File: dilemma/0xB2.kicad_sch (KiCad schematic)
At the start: 106 parts, among them J1 USB_C_Receptacle_USB2.0, J101 trackball, J102 Serial, J103 Serial, J104 BATTERY_CONN_DEANS, J105 S3B-PH-SM4-TB(LF)(SN), J106 S3B-PH-SM4-TB(LF)(SN), J107 Conn_01x08_Female, J113 Cirque, J5 Conn_01x02, SW1 SW_Push, SW101 SW_Push, SW102 SW_Push, SW103 SW_Push, SW104 SW_Push, SW105 SW_Push, SW106 SW_Push, SW107 SW_Push, SW108 SW_Push, SW109 SW_Push, SW110 SW_SPST, SW111 SW_SPST, SW112 SW_Push, SW113 SW_Push, SW114 SW_Push, SW115 SW_Push, SW116 SW_Push, SW117 SW_Push, SW118 SW_Push, SW119 SW_Push, SW2 SW_Push, U1 RP2040, U2 GD25Q80CEIGR, U3 XC6210B332MR-G, Y1 Crystal_GND24

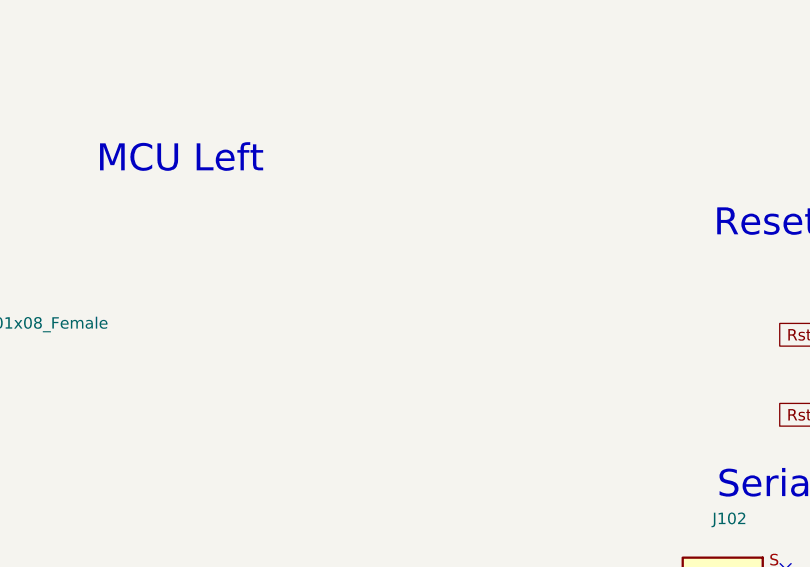
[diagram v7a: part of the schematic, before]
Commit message: add breakout pad for gpio2
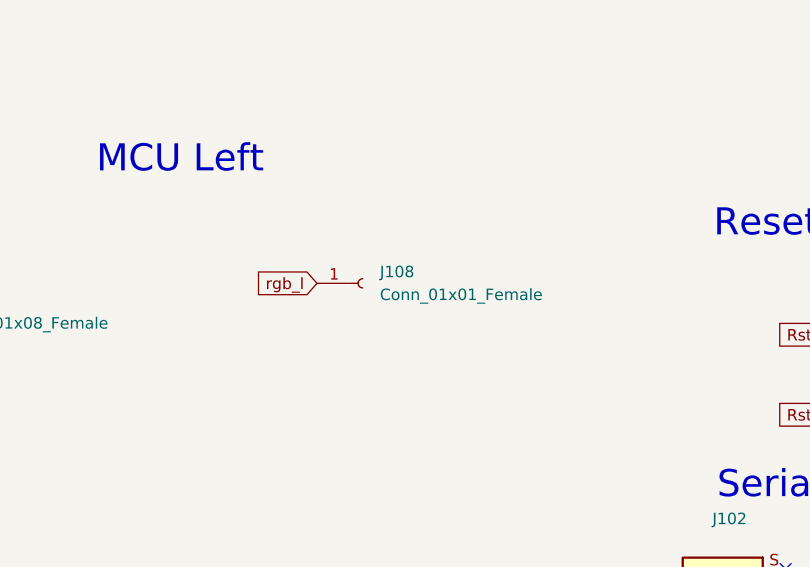
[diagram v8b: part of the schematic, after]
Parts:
- added J108: Conn_01x01_Female, Connector_Wire:SolderWirePad_1x01_SMD_1x2mm, symbol Connector:Conn_01x01_Female
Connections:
- net rgb_l: now also J108.1 (Pin_1)
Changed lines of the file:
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@@
+    )
+  )
+  (global_label "rgb_l" (shape input) (at 387.985 96.52 180)
+    (effects (font (size 1.27 1.27)) (justify right))
+    (property "Intersheet References" "${INTERSHEET_REFS}" (id 0) (at 300.355 29.21 0)
+      (effects (font (size 1.27 1.27)) hide)
     )
   )
@@
     (pin "2")
   )
+  (symbol (lib_id "Connector:Conn_01x01_Female") (at 393.065 96.52 0) (unit 1)
+    (in_bom yes) (on_board yes) (fields_autoplaced)
+    (property "Reference" "J108" (id 0) (at 394.97 95.2499 0)
+      (effects (font (size 1.27 1.27)) (justify left))
+    )
+    (property "Value" "Conn_01x01_Female" (id 1) (at 394.97 97.7899 0)
+      (effects (font (size 1.27 1.27)) (justify left))
+    )
+    (property "Footprint" "Connector_Wire:SolderWirePad_1x01_SMD_1x2mm" (id 2) (at 393.065 96.52 0)
+      (effects (font (size 1.27 1.27)) hide)
+    )
+    (property "Datasheet" "~" (id 3) (at 393.065 96.52 0)
+      (effects (font (size 1.27 1.27)) hide)
+    )
+    (pin "1")
+  )
   (symbol (lib_id "power:GND") (at 607.695 34.925 0) (unit 1)
     (in_bom yes) (on_board yes)
@@
       (reference "J107") (unit 1) (value "Conn_01x08_Female") (footprint "local-libraries:1x08 smd reversible")
     )
+    (path "/9ba28921-4e7a-475b-95b0-d10633adccee"
+      (reference "J108") (unit 1) (value "Conn_01x01_Female") (footprint "Connector_Wire:SolderWirePad_1x01_SMD_1x2mm")
+    )
     (path "/eeb6b826-bc65-4571-ab3b-1b47a831da34"
